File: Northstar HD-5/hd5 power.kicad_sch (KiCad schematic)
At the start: 42 parts, among them J1 MFM data, J2 MFM control, P1 northstar card edge, U1C 74S10, U1D 74S00, U1F 74S04, U1H 74LS123, U1K LM393, U1L 7438, U2C 74LS74, U2J 74LS393, U2K 74LS393, U3A 74S74, U3B 74S02, U3D 74LS04, U3F 74LS393, U4A 74S74, U4B 74S02, U4C 74S74, U4D 74S04, U4J 74LS04, U5F 74S74, U5H 74LS32, U5J 74LS00, U5K 74LS279

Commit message: changes to hd-5 and gitignore
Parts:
- C1, C2, C7: footprint Capacitor_THT:CP_Radial_D5.0mm_P2.50mm -> Capacitor_THT:CP_Radial_Tantal_D5.0mm_P2.50mm
- C13: footprint (none) -> Capacitor_THT:C_Disc_D10.0mm_W2.5mm_P5.00mm
- C15, C21: renamed from C?; value * -> 47nF; footprint Capacitor_THT:C_Disc_D7.5mm_W2.5mm_P5.00mm -> Capacitor_THT:C_Disc_D10.0mm_W2.5mm_P5.00mm
- C16: renamed from C?; footprint (none) -> Capacitor_THT:C_Disc_D10.0mm_W2.5mm_P5.00mm
- J1: footprint (none) -> Connector_PinHeader_2.54mm:PinHeader_2x10_P2.54mm_Horizontal
- J2: footprint (none) -> Connector_PinHeader_2.54mm:PinHeader_2x17_P2.54mm_Horizontal
- R1, R2, R3, R4: footprint Resistor_THT:R_Axial_DIN0207_L6.3mm_D2.5mm_P15.24mm_Horizontal -> Resistor_THT:R_Axial_DIN0309_L9.0mm_D3.2mm_P12.70mm_Horizontal
- RN1: footprint Resistor_THT:R_Array_SIP8 -> Package_SIP:SIP-8_19x3mm_P2.54mm
- RN2: renamed from RN?; footprint Resistor_THT:R_Array_SIP9 -> Package_SIP:SIP-9_21.54x3mm_P2.54mm
- TP5, TP7, TP8: footprint Connector_Pin:Pin_D1.0mm_L10.0mm -> Connector_PinHeader_2.54mm:PinHeader_1x01_P2.54mm_Vertical
- U1C1: renamed from U1C; footprint (none) -> Package_DIP:DIP-14_W7.62mm
- U1D1: renamed from U1D; footprint (none) -> Package_DIP:DIP-14_W7.62mm
- U1F1: renamed from U1F; footprint (none) -> Package_DIP:DIP-14_W7.62mm
- U1H1: renamed from U1H; footprint (none) -> Package_DIP:DIP-16_W7.62mm
- U1K1: renamed from U1K; footprint (none) -> Package_DIP:DIP-8-16_W7.62mm
- U1L1: renamed from U1L; footprint (none) -> Package_DIP:DIP-14_W7.62mm
- U2C1: renamed from U2C; footprint (none) -> Package_DIP:DIP-14_W7.62mm
- U2J1: renamed from U2J; footprint (none) -> Package_DIP:DIP-14_W7.62mm
- U2K1: renamed from U2K; footprint (none) -> Package_DIP:DIP-14_W7.62mm
- U3A1: renamed from U3A; footprint (none) -> Package_DIP:DIP-14_W7.62mm
- U3B1: renamed from U3B; footprint (none) -> Package_DIP:DIP-14_W7.62mm
- U3D1: renamed from U3D; footprint (none) -> Package_DIP:DIP-14_W7.62mm
- U3F1: renamed from U3F; footprint (none) -> Package_DIP:DIP-14_W7.62mm
- U4A1: renamed from U4A; footprint (none) -> Package_DIP:DIP-14_W7.62mm
- U4B1: renamed from U4B; footprint (none) -> Package_DIP:DIP-14_W7.62mm
- U4C1: renamed from U4C; footprint (none) -> Package_DIP:DIP-14_W7.62mm
- U4D1: renamed from U4D; footprint (none) -> Package_DIP:DIP-14_W7.62mm
- U4J1: renamed from U4J; footprint (none) -> Package_DIP:DIP-14_W7.62mm
- U5F1: renamed from U5F; footprint (none) -> Package_DIP:DIP-14_W7.62mm
- U5H1: renamed from U5H; footprint (none) -> Package_DIP:DIP-14_W7.62mm
- U5J1: renamed from U5J; footprint (none) -> Package_DIP:DIP-14_W7.62mm
- U5K1: renamed from U5K; footprint (none) -> Package_DIP:DIP-16_W7.62mm
- VR1: renamed from VR?; footprint Package_TO_SOT_THT:TO-220-3_Vertical -> Package_TO_SOT_THT:TO-220-3_Horizontal_TabDown

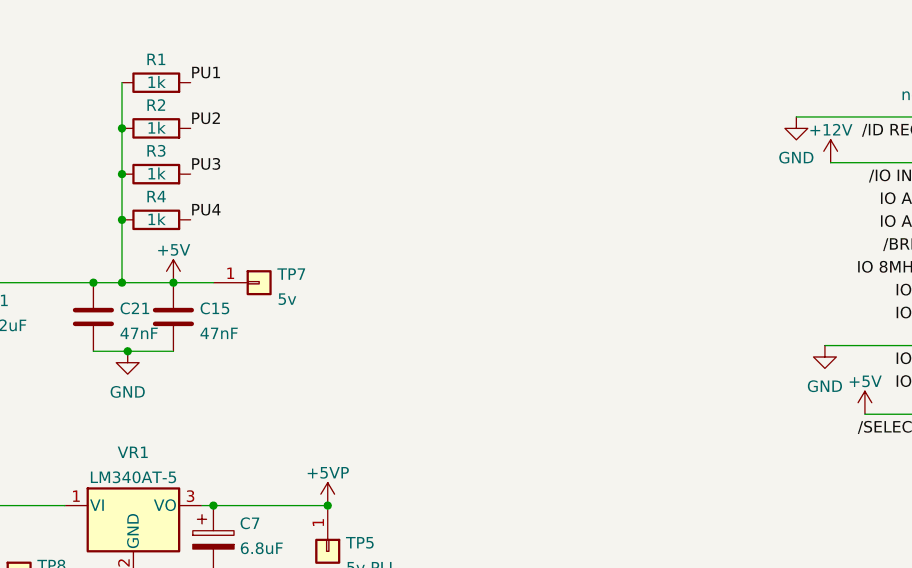
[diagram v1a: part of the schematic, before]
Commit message: placed components for column 5
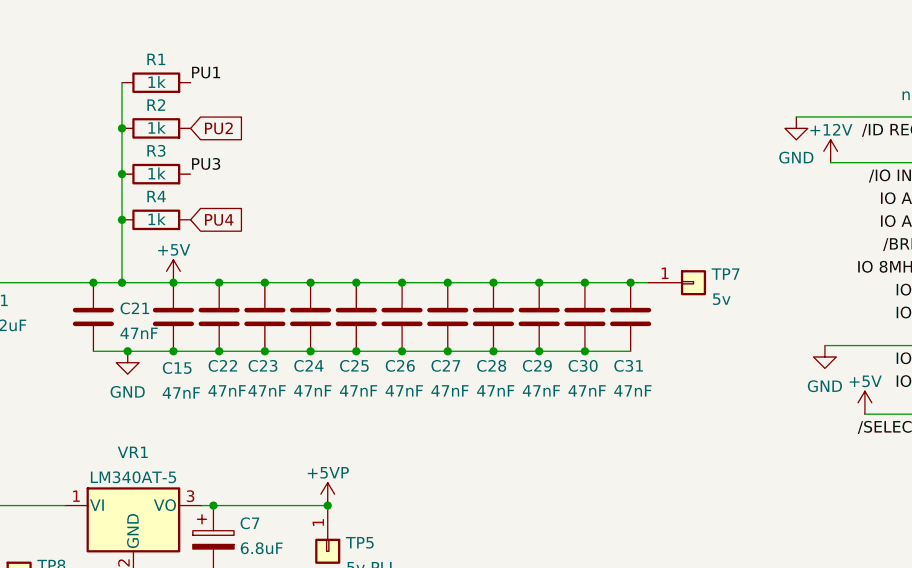
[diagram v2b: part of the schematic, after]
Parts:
- added C22, C23, C24, C25, C26, C27, C28, C29, C30, C31: 47nF, Capacitor_THT:C_Disc_D10.0mm_W2.5mm_P5.00mm, symbol Device:C
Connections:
- net +5V: now also C22.1, C23.1, C24.1, C25.1, C26.1, C27.1, C28.1, C29.1, C30.1, C31.1
- net GND: now also C22.2, C23.2, C24.2, C25.2, C26.2, C27.2, C28.2, C29.2, C30.2, C31.2
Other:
- moved on the sheet: TP7

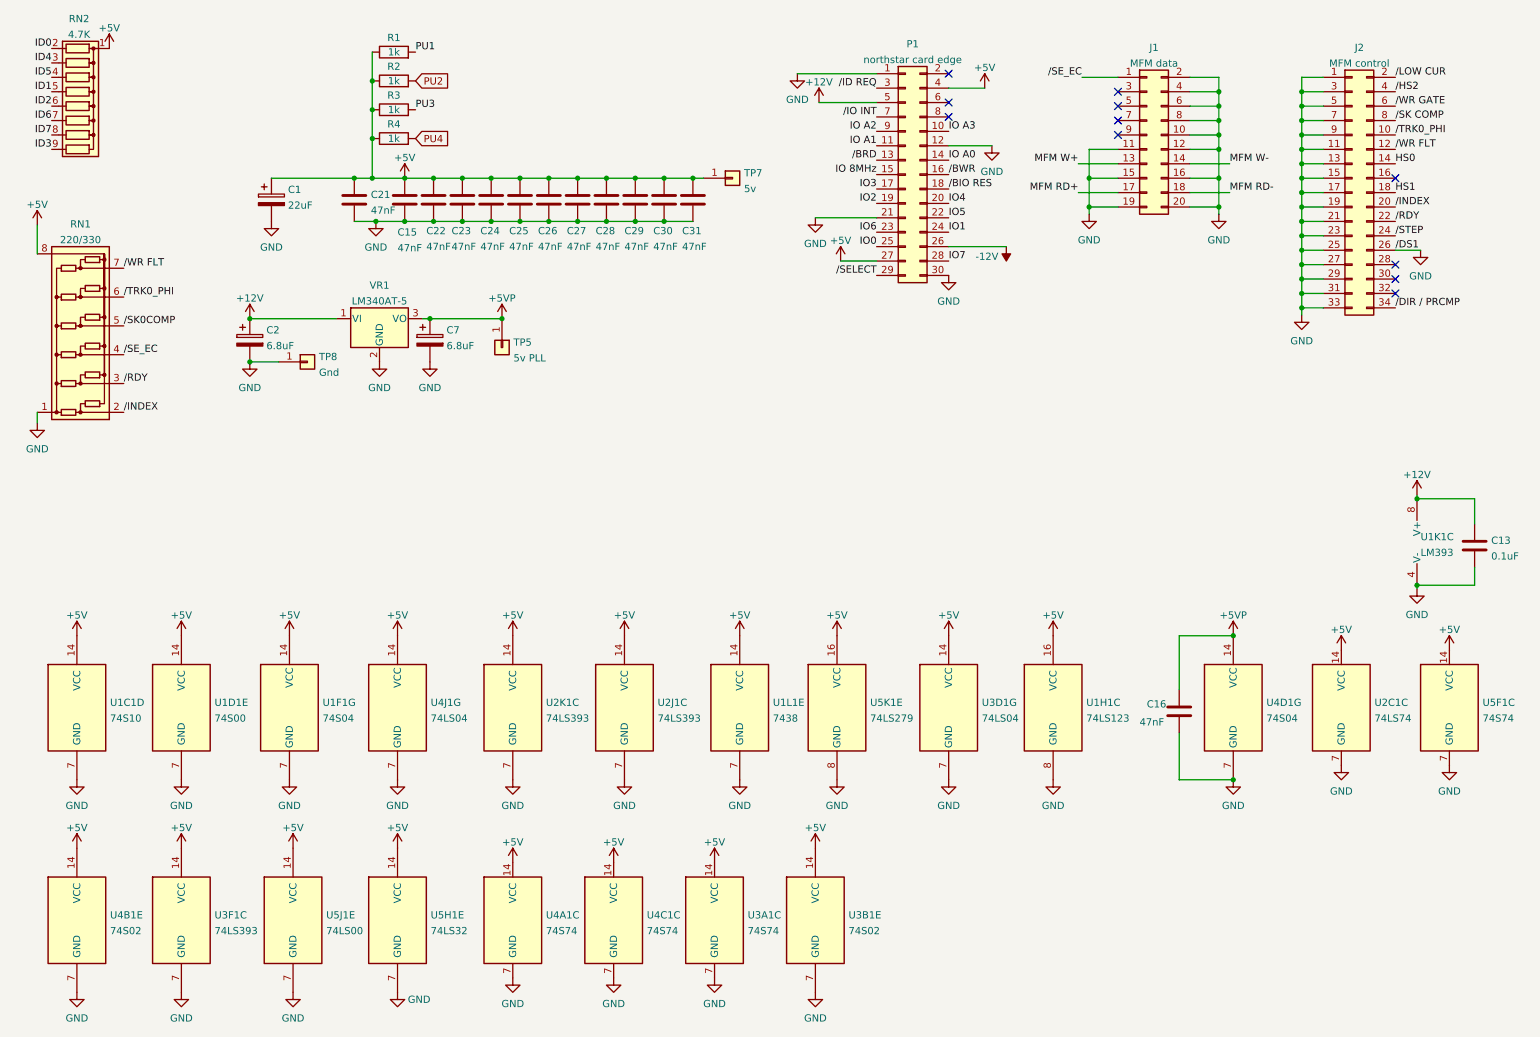
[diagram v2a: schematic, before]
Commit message: placed components and repaired multi sheet labels
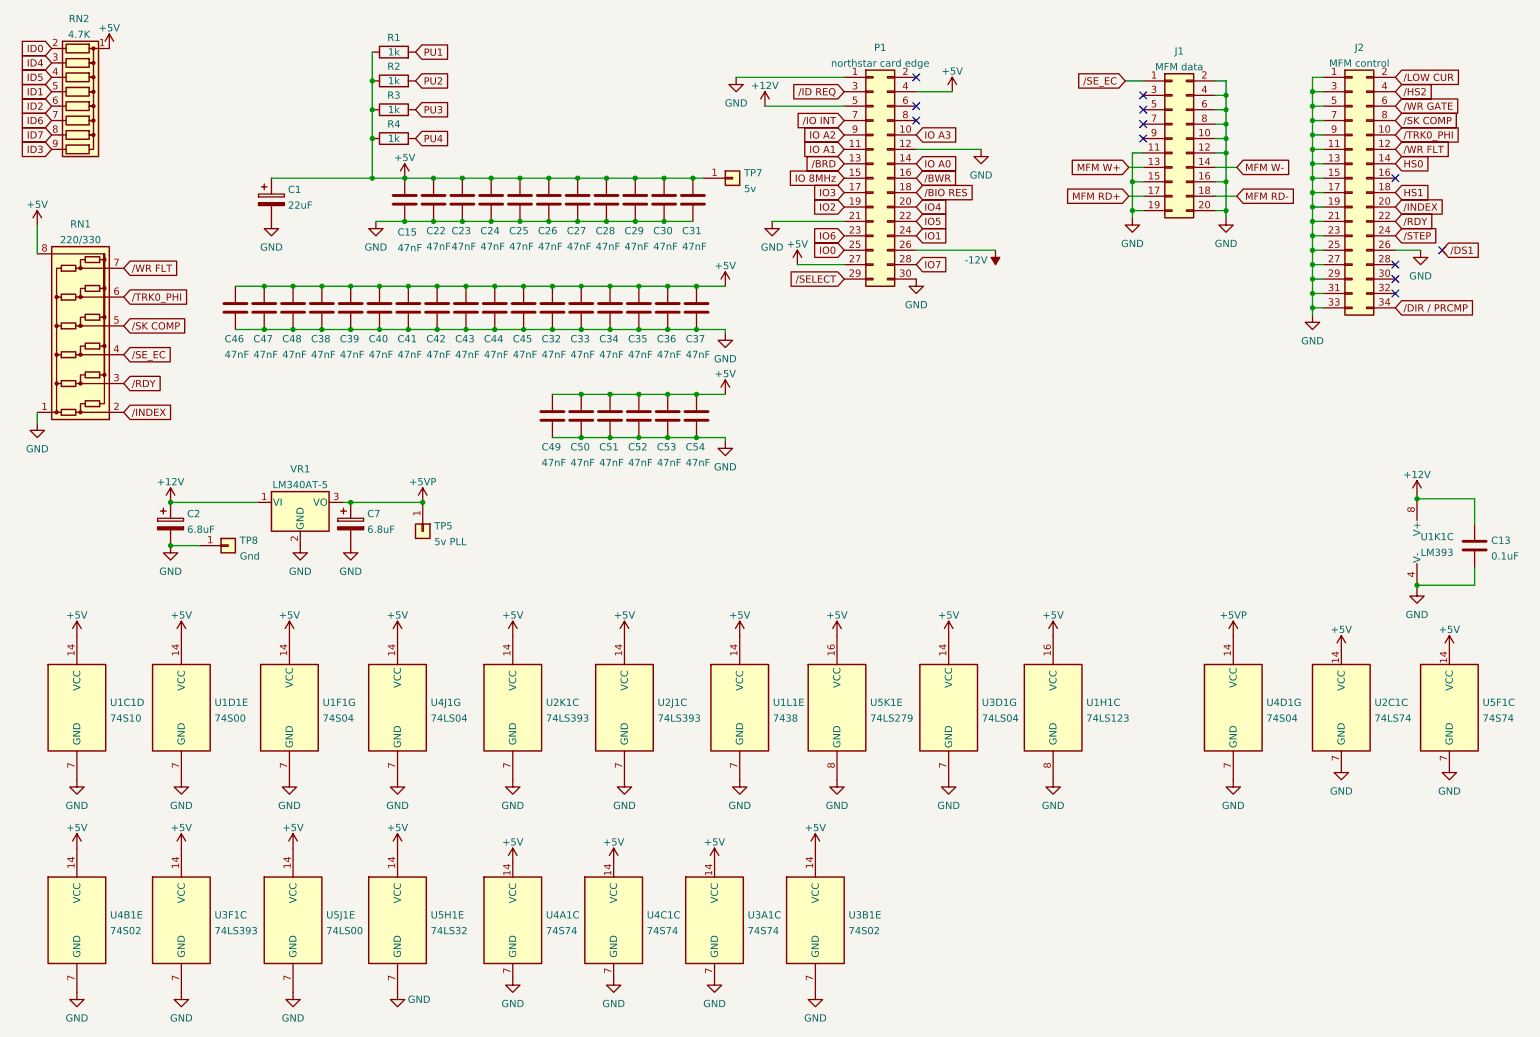
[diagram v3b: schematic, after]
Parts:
- removed C16, C21: 47nF, Capacitor_THT:C_Disc_D10.0mm_W2.5mm_P5.00mm, symbol Device:C
- added C32, C33, C34, C35, C36, C37, C38, C39, C40, C41, C42, C43, C44, C45, C46, C47, C48, C49, C50, C51, C52, C53, C54: 47nF, Capacitor_THT:C_Disc_D10.0mm_W2.5mm_P5.00mm, symbol Device:C
- U1K1: footprint Package_DIP:DIP-8-16_W7.62mm -> Package_DIP:DIP-8_W7.62mm
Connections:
- net /SK0COMP is gone; now on net /SK COMP: RN1.5 (R4)
- net +5V: now also C32.1, C33.1, C34.1, C35.1, C36.1, C37.1, C38.1, C39.1, C40.1, C41.1, C42.1, C43.1, C44.1, C45.1, C46.1, C47.1, C48.1, C49.1, C50.1, C51.1, C52.1, C53.1, C54.1
- net GND: now also C32.2, C33.2, C34.2, C35.2, C36.2, C37.2, C38.2, C39.2, C40.2, C41.2, C42.2, C43.2, C44.2, C45.2, C46.2, C47.2, C48.2, C49.2, C50.2, C51.2, C52.2, C53.2, C54.2
- no-connect marks 11 -> 12
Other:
- moved on the sheet: C2, C7, J1, P1, TP5, TP8, VR1

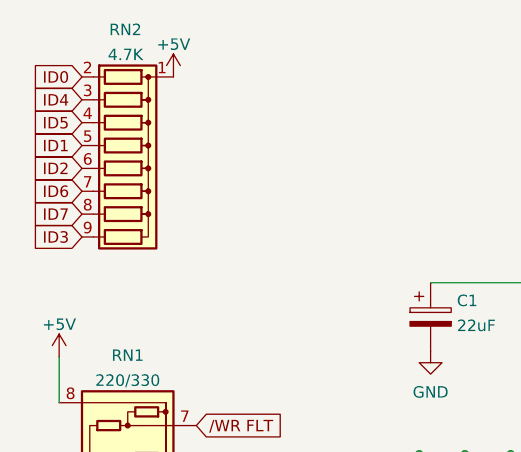
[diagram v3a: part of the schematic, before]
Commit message: finished signal routing top and bottom (assumed correct)
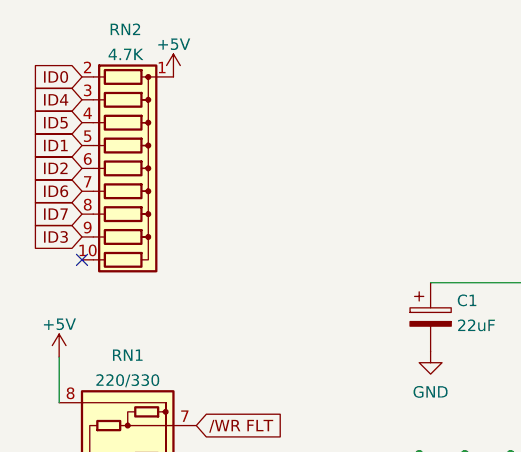
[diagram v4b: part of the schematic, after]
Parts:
- removed RN2: 4.7K, Package_SIP:SIP-9_21.54x3mm_P2.54mm, symbol Device:R_Network08
- added RN2: 4.7K, Resistor_THT:R_Array_SIP10, symbol Device:R_Network09
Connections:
- net +5V: now also RN2.1 (common)
- net ID0: now also RN2.2 (R1)
- net ID1: now also RN2.5 (R4)
- net ID2: now also RN2.6 (R5)
- net ID3: now also RN2.9 (R8)
- net ID4: now also RN2.3 (R2)
- net ID5: now also RN2.4 (R3)
- net ID6: now also RN2.7 (R6)
- net ID7: now also RN2.8 (R7)
- no-connect marks 12 -> 13
